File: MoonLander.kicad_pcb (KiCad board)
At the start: 2 copper layers, 37.8 x 22.7 mm, 46 parts, among them IC1 MCP73831/2, IC2 BU33SD5, IC3 PRTR5V0U2X, IC4 CP2110-GM, IC5 LPC824M201JHI33, J1 Cortex_JTAG/SWD_10, P1 CONN_01X02, P2 CONN_01X02, P3 USB_OTG, P4 CONN_02X08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

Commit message: moved a few things
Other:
- board text added: "+"
- board text added: "-"
- board text added: "3V3"
- board text added: "CHG"
- board text added: "GND"
- board text added: "IO1"
- board text added: "IO10"
- board text added: "IO2"
- board text added: "IO3"
- board text added: "IO4"
- board text added: "IO5"
- board text added: "IO6"
- board text added: "IO7"
- board text added: "IO8"
- board text added: "IO9"
- board text added: "RST"
- board text added: "SCL"
- board text added: "SDA"
- board text added: "SWD"
- board text added: "VIN"
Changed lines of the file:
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@@
     (area 129.210999 86.665999 167.207001 109.549001)
     (thickness 1.6)
-    (drawings 16)
+    (drawings 36)
     (tracks 467)
     (zones 0)
@@
     (tags "capacitor 0402")
     (attr smd)
-    (fp_text reference C5 (at 1.651 0 270) (layer F.SilkS)
+    (fp_text reference C5 (at 1.524 0 270) (layer F.SilkS)
       (effects (font (size 0.65 0.65) (thickness 0.1)))
     )
@@
     (tags "capacitor 0402")
     (attr smd)
-    (fp_text reference C8 (at -1.651 0 90) (layer F.SilkS)
+    (fp_text reference C8 (at -1.524 0 90) (layer F.SilkS)
       (effects (font (size 0.65 0.65) (thickness 0.1)))
     )
@@
     (tags "capacitor 0402")
     (attr smd)
-    (fp_text reference C10 (at 1.905 0 90) (layer F.SilkS)
+    (fp_text reference C10 (at -1.905 0.127 90) (layer F.SilkS)
       (effects (font (size 0.65 0.65) (thickness 0.1)))
     )
@@
     (tags "capacitor 0402")
     (attr smd)
-    (fp_text reference C11 (at 0 -1.7 270) (layer F.SilkS)
+    (fp_text reference C11 (at 0 1.016 270) (layer F.SilkS)
       (effects (font (size 0.65 0.65) (thickness 0.1)))
     )
@@
     (tags "LED led 0603 SMD smd SMT smt smdled SMDLED smtled SMTLED")
     (attr smd)
-    (fp_text reference D1 (at 2.032 0 270) (layer F.SilkS)
+    (fp_text reference D1 (at 1.778 0 270) (layer F.SilkS)
       (effects (font (size 0.65 0.65) (thickness 0.1)))
     )
@@
     (tags SOD-323)
     (attr smd)
-    (fp_text reference D2 (at 0 -1.524 180) (layer F.SilkS)
+    (fp_text reference D2 (at -0.381 -1.397 180) (layer F.SilkS)
       (effects (font (size 0.65 0.65) (thickness 0.1)))
     )
@@
     (tags "QFN 0.5")
     (attr smd)
-    (fp_text reference IC5 (at 0 -3.75 270) (layer F.SilkS)
+    (fp_text reference IC5 (at 0.8625 -3.5295 270) (layer F.SilkS)
       (effects (font (size 0.65 0.65) (thickness 0.1)))
     )
@@
     (descr "Through hole socket strip")
     (tags "socket strip")
-    (fp_text reference P1 (at 4.572 -0.127 540) (layer F.SilkS)
+    (fp_text reference P1 (at 3.81 -2.159 360) (layer F.SilkS)
       (effects (font (size 0.65 0.65) (thickness 0.1)))
     )
@@
     (tags "USB USB_B USB_micro USB_OTG")
     (attr smd)
-    (fp_text reference P3 (at -5.0809 -1.68954 360) (layer F.SilkS)
+    (fp_text reference P3 (at 5.1435 -0.508 360) (layer F.SilkS)
       (effects (font (size 0.65 0.65) (thickness 0.1)))
     )
@@
     (tags "resistor 0402")
     (attr smd)
-    (fp_text reference R10 (at -1.974 0 270) (layer F.SilkS)
+    (fp_text reference R10 (at 1.709 -0.254 270) (layer F.SilkS)
       (effects (font (size 0.65 0.65) (thickness 0.1)))
     )
@@
     (at 154.94 103.251)
     (descr "crystal Epson Toyocom FA-238 and TSX-3225 series")
-    (fp_text reference Y1 (at 0.17 1.905) (layer F.SilkS)
+    (fp_text reference Y1 (at -1.016 -1.905) (layer F.SilkS)
       (effects (font (size 0.65 0.65) (thickness 0.1)))
     )
@@
   (module GrayCatLabs:Header_2mm_2x6 (layer F.Cu)
     (at 165.703 107.918 90)
-    (fp_text reference P4 (at 3.968 -3.302 270) (layer F.SilkS)
+    (fp_text reference P4 (at 13.43 -1.746 360) (layer F.SilkS)
       (effects (font (size 1 1) (thickness 0.15)))
     )
@@
       (net 2 GND))
   )
+  (gr_text SCL (at 166.751 95.885 90) (layer F.SilkS)
+    (effects (font (size 0.5 0.5) (thickness 0.1)))
+  )
+  (gr_text SDA (at 162.687 95.885 90) (layer F.SilkS)
+    (effects (font (size 0.5 0.5) (thickness 0.1)))
+  )
+  (gr_text IO10 (at 166.751 97.917 90) (layer F.SilkS)
+    (effects (font (size 0.5 0.5) (thickness 0.1)))
+  )
+  (gr_text IO9 (at 162.687 97.917 90) (layer F.SilkS)
+    (effects (font (size 0.5 0.5) (thickness 0.1)))
+  )
+  (gr_text IO7 (at 162.687 99.949 90) (layer F.SilkS)
+    (effects (font (size 0.5 0.5) (thickness 0.1)))
+  )
+  (gr_text IO8 (at 166.751 99.949 90) (layer F.SilkS)
+    (effects (font (size 0.5 0.5) (thickness 0.1)))
+  )
+  (gr_text IO6 (at 166.751 101.854 90) (layer F.SilkS)
+    (effects (font (size 0.5 0.5) (thickness 0.1)))
+  )
+  (gr_text IO5 (at 162.687 101.854 90) (layer F.SilkS)
+    (effects (font (size 0.5 0.5) (thickness 0.1)))
+  )
+  (gr_text IO4 (at 166.751 103.886 90) (layer F.SilkS)
+    (effects (font (size 0.5 0.5) (thickness 0.1)))
+  )
+  (gr_text IO3 (at 162.687 103.886 90) (layer F.SilkS)
+    (effects (font (size 0.5 0.5) (thickness 0.1)))
+  )
+  (gr_text IO1 (at 162.687 105.918 90) (layer F.SilkS)
+    (effects (font (size 0.5 0.5) (thickness 0.1)))
+  )
+  (gr_text GND (at 162.687 107.95 90) (layer F.SilkS)
+    (effects (font (size 0.5 0.5) (thickness 0.1)))
+  )
+  (gr_text 3V3 (at 166.751 107.95 90) (layer F.SilkS)
+    (effects (font (size 0.5 0.5) (thickness 0.1)))
+  )
+  (gr_text IO2 (at 166.751 105.918 90) (layer F.SilkS)
+    (effects (font (size 0.5 0.5) (thickness 0.1)))
+  )
+  (gr_text SWD (at 153.797 105.41) (layer F.SilkS)
+    (effects (font (size 1 1) (thickness 0.125)))
+  )
+  (gr_text RST (at 162.687 92.075 90) (layer F.SilkS)
+    (effects (font (size 1 1) (thickness 0.125)))
+  )
+  (gr_text VIN (at 130.683 92.583 360) (layer F.SilkS)
+    (effects (font (size 1 1) (thickness 0.125)))
+  )
+  (gr_text - (at 132.461 90.424 90) (layer F.SilkS)
+    (effects (font (size 1 1) (thickness 0.125)))
+  )
+  (gr_text + (at 132.588 88.011) (layer F.SilkS)
+    (effects (font (size 1 1) (thickness 0.125)))
+  )
+  (gr_text CHG (at 134.874 88.265) (layer F.SilkS)
+    (effects (font (size 1 1) (thickness 0.125)))
+  )
   (dimension 22.733 (width 0.2) (layer Dwgs.User)
     (gr_text "0.8950 in" (at 174.126 98.1075 90) (layer Dwgs.User)
@@
   )
   (dimension 37.846 (width 0.2) (layer Dwgs.User)
-    (gr_text "1.4900 in" (at 148.209 118.881) (layer Dwgs.User)
+    (gr_text "1.4900 in" (at 148.209 116.976) (layer Dwgs.User)
       (effects (font (size 1.25 1.25) (thickness 0.2)))
     )
-    (feature1 (pts (xy 129.286 109.474) (xy 129.286 119.906)))
-    (feature2 (pts (xy 167.132 109.474) (xy 167.132 119.906)))
-    (crossbar (pts (xy 167.132 117.856) (xy 129.286 117.856)))
-    (arrow1a (pts (xy 129.286 117.856) (xy 130.412504 117.269579)))
-    (arrow1b (pts (xy 129.286 117.856) (xy 130.412504 118.442421)))
-    (arrow2a (pts (xy 167.132 117.856) (xy 166.005496 117.269579)))
-    (arrow2b (pts (xy 167.132 117.856) (xy 166.005496 118.442421)))
+    (feature1 (pts (xy 129.286 109.474) (xy 129.286 118.001)))
+    (feature2 (pts (xy 167.132 109.474) (xy 167.132 118.001)))
+    (crossbar (pts (xy 167.132 115.951) (xy 129.286 115.951)))
+    (arrow1a (pts (xy 129.286 115.951) (xy 130.412504 115.364579)))
+    (arrow1b (pts (xy 129.286 115.951) (xy 130.412504 116.537421)))
+    (arrow2a (pts (xy 167.132 115.951) (xy 166.005496 115.364579)))
+    (arrow2b (pts (xy 167.132 115.951) (xy 166.005496 116.537421)))
   )
   (gr_line (start 129.286 109.474) (end 129.286 86.741) (layer Edge.Cuts) (width 0.15))

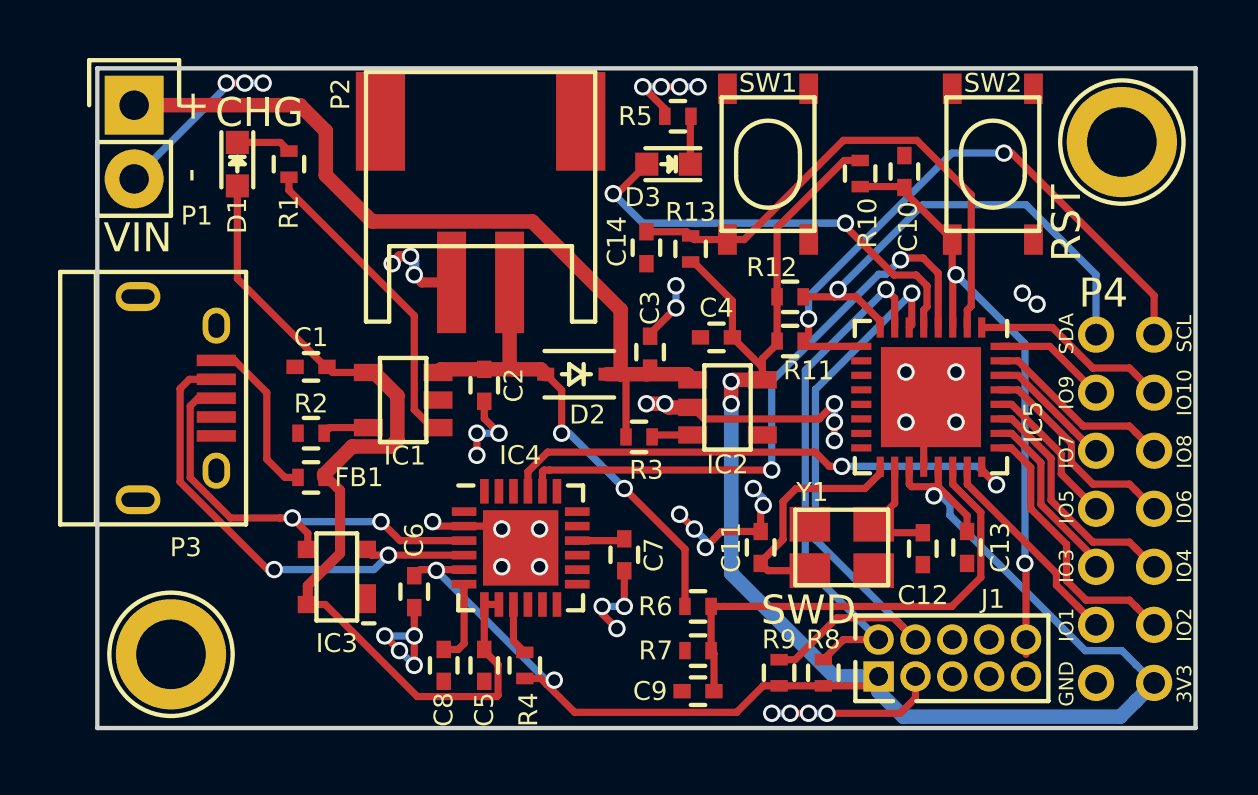
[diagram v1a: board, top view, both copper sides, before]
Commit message: switched microUSB footprint
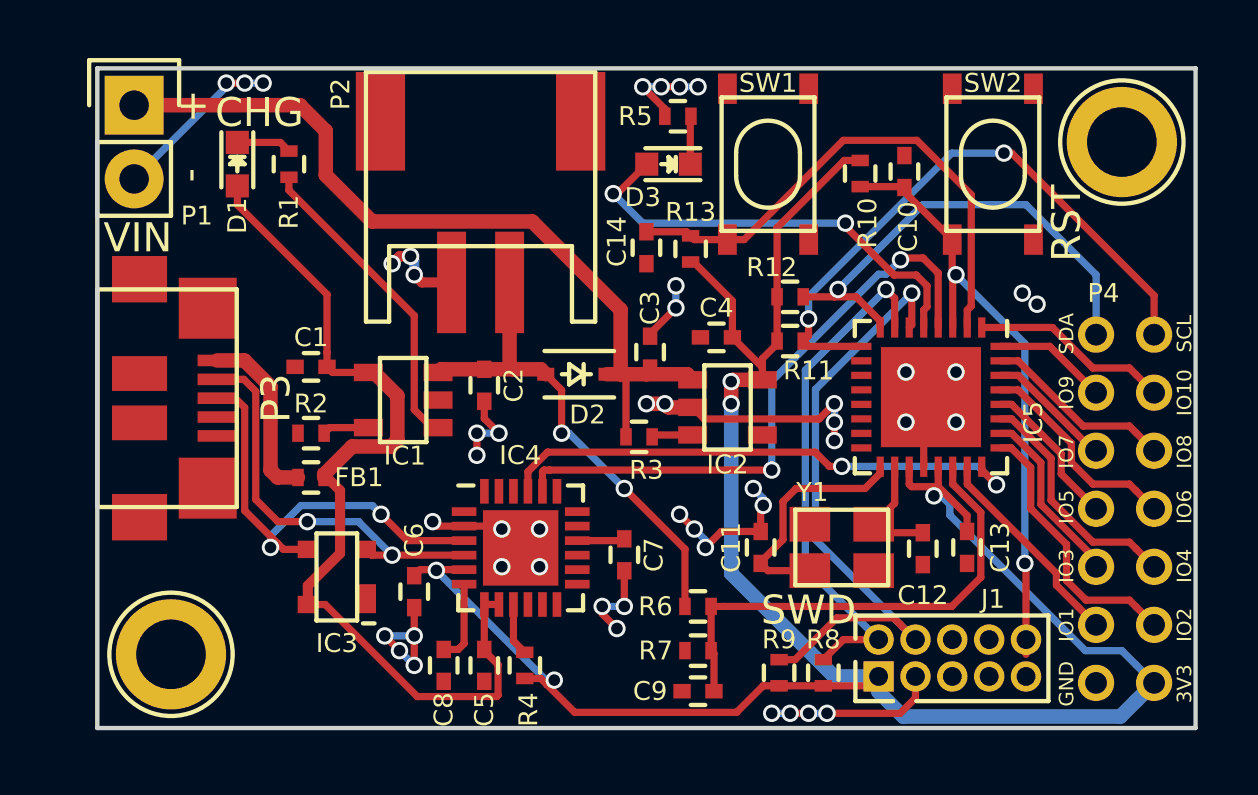
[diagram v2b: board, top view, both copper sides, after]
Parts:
- P3: footprint Connect:USB_Micro-B -> GrayCatLabs:ZX62R-B-5P
- moved P3 1.33 mm to (130.5, 98.1), turned to 180 degrees
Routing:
- net /USB-Serial/USB_D-: track 16.7 -> 14.2 mm
- net /USB-Serial/USB_D+: track 15.1 -> 15.7 mm
